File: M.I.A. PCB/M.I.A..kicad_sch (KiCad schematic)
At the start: 44 parts, among them J1 USB_C_Receptacle_USB2.0_16P, SW1 SW_Push, SW2 SW_Push, U1 W25Q128JVS, U2 RP2350B-QFN80, Y1 ABM8-272-T3

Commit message: Routing Updates
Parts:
- R2, R3: value 27 -> 33
- R6: value 270 -> 330
- R7, R8: value 4.7k -> 5.1k
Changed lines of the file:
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@@
 			)
 		)
-		(property "Value" "27"
+		(property "Value" "33"
 			(at 184.15 37.084 90)
 			(effects
@@
 			)
 		)
-		(property "Value" "4.7k"
+		(property "Value" "5.1k"
 			(at 208.28 128.2699 0)
 			(effects
@@
 			)
 		)
-		(property "Value" "4.7k"
+		(property "Value" "5.1k"
 			(at 218.44 128.2699 0)
 			(effects
@@
 			)
 		)
-		(property "Value" "270"
+		(property "Value" "330"
 			(at 215.9 107.95 90)
 			(effects
@@
 			)
 		)
-		(property "Value" "27"
+		(property "Value" "33"
 			(at 184.15 46.736 90)
 			(effects

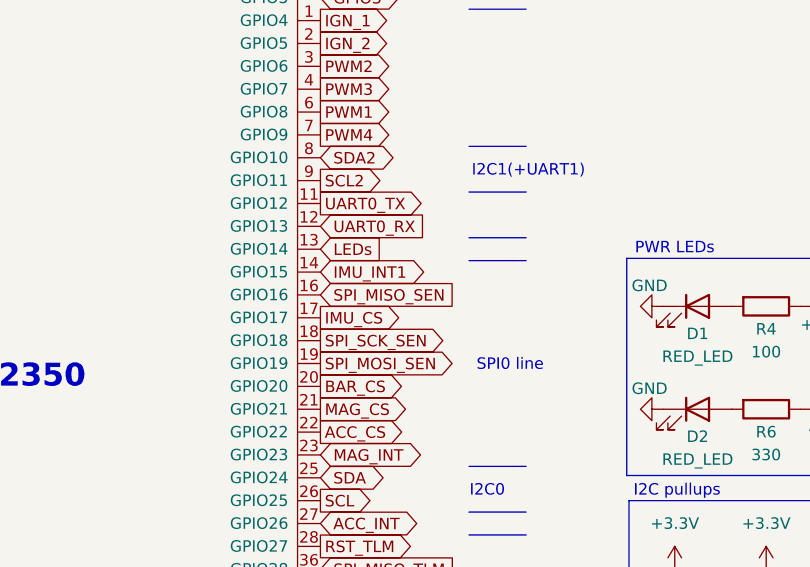
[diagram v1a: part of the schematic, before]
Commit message: Added Test Points + Back Graphics
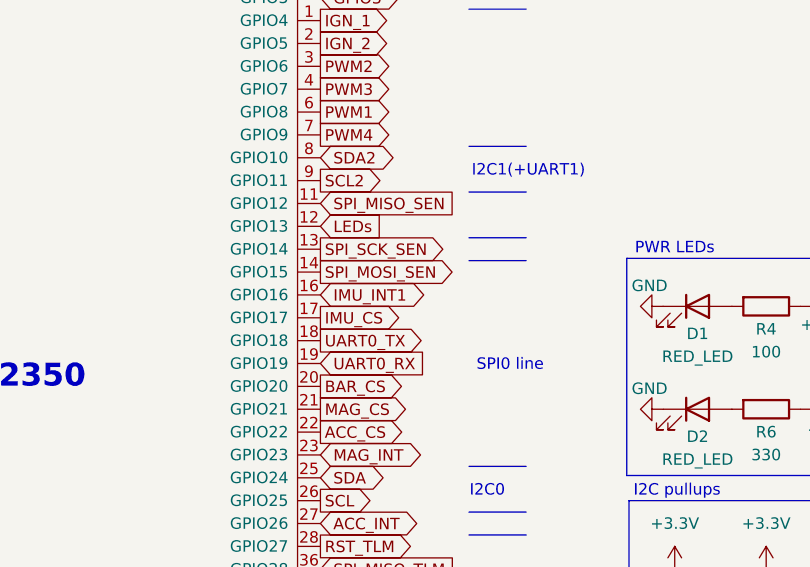
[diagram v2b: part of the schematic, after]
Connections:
- net IMU_INT1: now also U2.16 (GPIO16); no longer U2.14 (GPIO15)
- net LEDs: now also U2.12 (GPIO13); no longer U2.13 (GPIO14)
- net SPI_MISO_SEN: now also U2.11 (GPIO12); no longer U2.16 (GPIO16)
- net SPI_MOSI_SEN: now also U2.14 (GPIO15); no longer U2.19 (GPIO19)
- net SPI_SCK_SEN: now also U2.13 (GPIO14); no longer U2.18 (GPIO18)
- net UART0_RX: now also U2.19 (GPIO19); no longer U2.12 (GPIO13)
- net UART0_TX: now also U2.18 (GPIO18); no longer U2.11 (GPIO12)
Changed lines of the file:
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@@
 	(global_label "UART0_TX"
 		(shape output)
-		(at 166.37 80.01 0)
-		(fields_autoplaced yes)
-		(effects
-			(font
-				(size 1.27 1.27)
-			)
-			(justify left)
-		)
-		(property "Intersheetrefs" "${INTERSHEET_REFS}"
-			(at 178.3661 80.01 0)
+		(at 166.37 95.25 0)
+		(fields_autoplaced yes)
+		(effects
+			(font
+				(size 1.27 1.27)
+			)
+			(justify left)
+		)
+		(property "Intersheetrefs" "${INTERSHEET_REFS}"
+			(at 178.3661 95.25 0)
 			(effects
 				(font
@@
 	(global_label "UART0_RX"
 		(shape input)
-		(at 166.37 82.55 0)
-		(fields_autoplaced yes)
-		(effects
-			(font
-				(size 1.27 1.27)
-			)
-			(justify left)
-		)
-		(property "Intersheetrefs" "${INTERSHEET_REFS}"
-			(at 178.6685 82.55 0)
+		(at 166.37 97.79 0)
+		(fields_autoplaced yes)
+		(effects
+			(font
+				(size 1.27 1.27)
+			)
+			(justify left)
+		)
+		(property "Intersheetrefs" "${INTERSHEET_REFS}"
+			(at 178.6685 97.79 0)
 			(effects
 				(font
@@
 	(global_label "IMU_INT1"
 		(shape bidirectional)
-		(at 166.37 87.63 0)
-		(fields_autoplaced yes)
-		(effects
-			(font
-				(size 1.27 1.27)
-			)
-			(justify left)
-		)
-		(property "Intersheetrefs" "${INTERSHEET_REFS}"
-			(at 178.9332 87.63 0)
+		(at 166.37 90.17 0)
+		(fields_autoplaced yes)
+		(effects
+			(font
+				(size 1.27 1.27)
+			)
+			(justify left)
+		)
+		(property "Intersheetrefs" "${INTERSHEET_REFS}"
+			(at 178.9332 90.17 0)
 			(effects
 				(font
@@
 	(global_label "SPI_MISO_SEN"
 		(shape input)
-		(at 166.37 90.17 0)
-		(fields_autoplaced yes)
-		(effects
-			(font
-				(size 1.27 1.27)
-			)
-			(justify left)
-		)
-		(property "Intersheetrefs" "${INTERSHEET_REFS}"
-			(at 182.6599 90.17 0)
+		(at 166.37 80.01 0)
+		(fields_autoplaced yes)
+		(effects
+			(font
+				(size 1.27 1.27)
+			)
+			(justify left)
+		)
+		(property "Intersheetrefs" "${INTERSHEET_REFS}"
+			(at 182.6599 80.01 0)
 			(effects
 				(font
@@
 	(global_label "LEDs"
 		(shape input)
+		(at 166.37 82.55 0)
+		(fields_autoplaced yes)
+		(effects
+			(font
+				(size 1.27 1.27)
+			)
+			(justify left)
+		)
+		(property "Intersheetrefs" "${INTERSHEET_REFS}"
+			(at 173.8304 82.55 0)
+			(effects
+				(font
+					(size 1.27 1.27)
+				)
+				(justify left)
+				(hide yes)
+			)
+		)
+	)
+	(global_label "Cont_Sense2"
+		(shape output)
+		(at 166.37 158.75 0)
+		(fields_autoplaced yes)
+		(effects
+			(font
+				(size 1.27 1.27)
+			)
+			(justify left)
+		)
+		(property "Intersheetrefs" "${INTERSHEET_REFS}"
+			(at 181.3898 158.75 0)
+			(effects
+				(font
+					(size 1.27 1.27)
+				)
+				(justify left)
+				(hide yes)
+			)
+		)
+	)
+	(global_label "PWM6"
+		(shape output)
+		(at 166.37 171.45 0)
+		(fields_autoplaced yes)
+		(effects
+			(font
+				(size 1.27 1.27)
+			)
+			(justify left)
+		)
+		(property "Intersheetrefs" "${INTERSHEET_REFS}"
+			(at 174.7375 171.45 0)
+			(effects
+				(font
+					(size 1.27 1.27)
+				)
+				(justify left)
+				(hide yes)
+			)
+		)
+	)
+	(global_label "SPI_SCK_SEN"
+		(shape output)
 		(at 166.37 85.09 0)
 		(fields_autoplaced yes)
@@
 		)
 		(property "Intersheetrefs" "${INTERSHEET_REFS}"
-			(at 173.8304 85.09 0)
-			(effects
-				(font
-					(size 1.27 1.27)
-				)
-				(justify left)
-				(hide yes)
-			)
-		)
-	)
-	(global_label "Cont_Sense2"
-		(shape output)
-		(at 166.37 158.75 0)
-		(fields_autoplaced yes)
-		(effects
-			(font
-				(size 1.27 1.27)
-			)
-			(justify left)
-		)
-		(property "Intersheetrefs" "${INTERSHEET_REFS}"
-			(at 181.3898 158.75 0)
-			(effects
-				(font
-					(size 1.27 1.27)
-				)
-				(justify left)
-				(hide yes)
-			)
-		)
-	)
-	(global_label "PWM6"
-		(shape output)
-		(at 166.37 171.45 0)
-		(fields_autoplaced yes)
-		(effects
-			(font
-				(size 1.27 1.27)
-			)
-			(justify left)
-		)
-		(property "Intersheetrefs" "${INTERSHEET_REFS}"
-			(at 174.7375 171.45 0)
-			(effects
-				(font
-					(size 1.27 1.27)
-				)
-				(justify left)
-				(hide yes)
-			)
-		)
-	)
-	(global_label "SPI_SCK_SEN"
-		(shape output)
-		(at 166.37 95.25 0)
-		(fields_autoplaced yes)
-		(effects
-			(font
-				(size 1.27 1.27)
-			)
-			(justify left)
-		)
-		(property "Intersheetrefs" "${INTERSHEET_REFS}"
-			(at 181.8132 95.25 0)
+			(at 181.8132 85.09 0)
 			(effects
 				(font
@@
 	(global_label "SPI_MOSI_SEN"
 		(shape output)
-		(at 166.37 97.79 0)
-		(fields_autoplaced yes)
-		(effects
-			(font
-				(size 1.27 1.27)
-			)
-			(justify left)
-		)
-		(property "Intersheetrefs" "${INTERSHEET_REFS}"
-			(at 182.6599 97.79 0)
-			(effects
-				(font
+		(at 166.37 87.63 0)
+		(fields_autoplaced yes)
+		(effects
+			(font
+				(size 1.27 1.27)
+			)
+			(justify left)
+		)
+		(property "Intersheetrefs" "${INTERSHEET_REFS}"
+			(at 182.6599 87.63 0)
+			(effects
+				(font
